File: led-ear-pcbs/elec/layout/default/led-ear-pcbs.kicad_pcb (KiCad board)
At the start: 2 copper layers, 225.7 x 100.8 mm, 0 parts

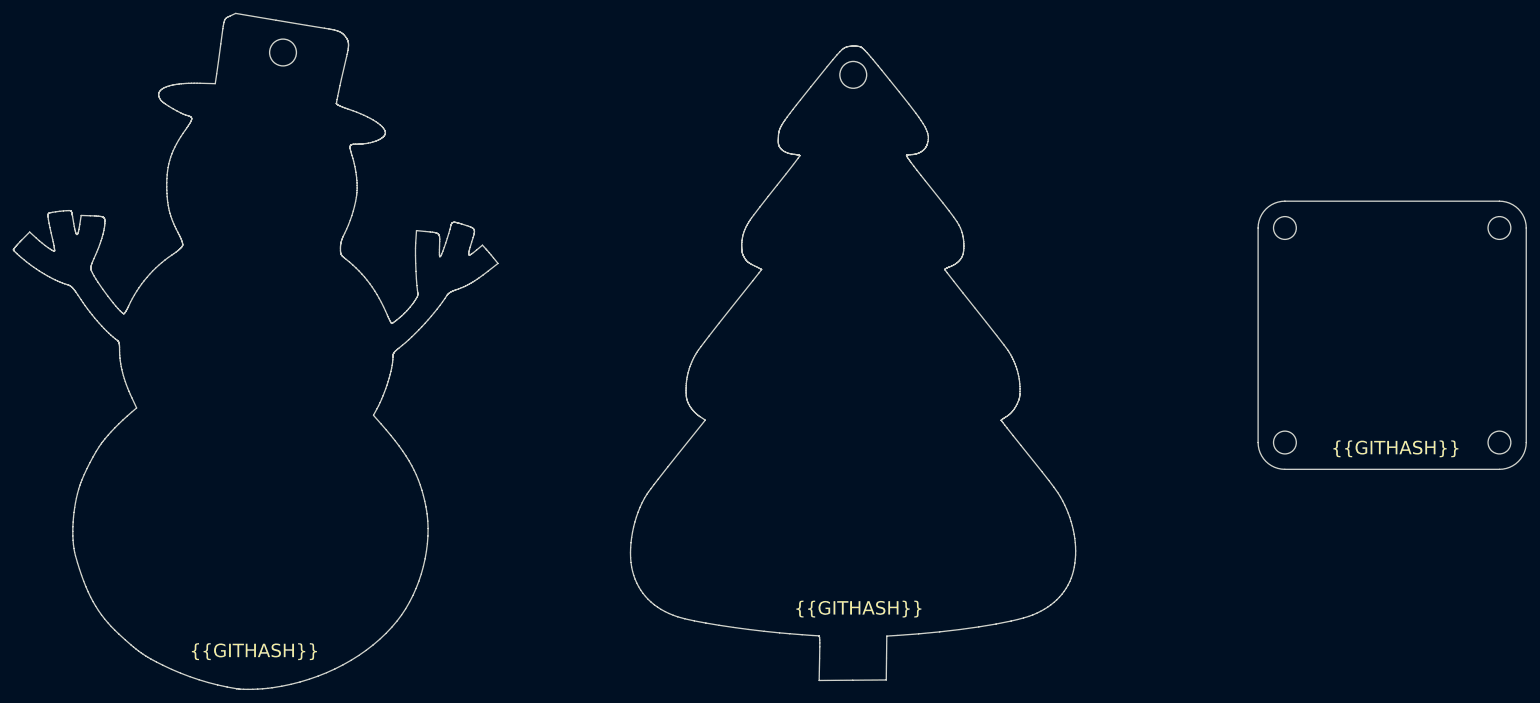
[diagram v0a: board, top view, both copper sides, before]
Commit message: added all components and specs, starting placing components
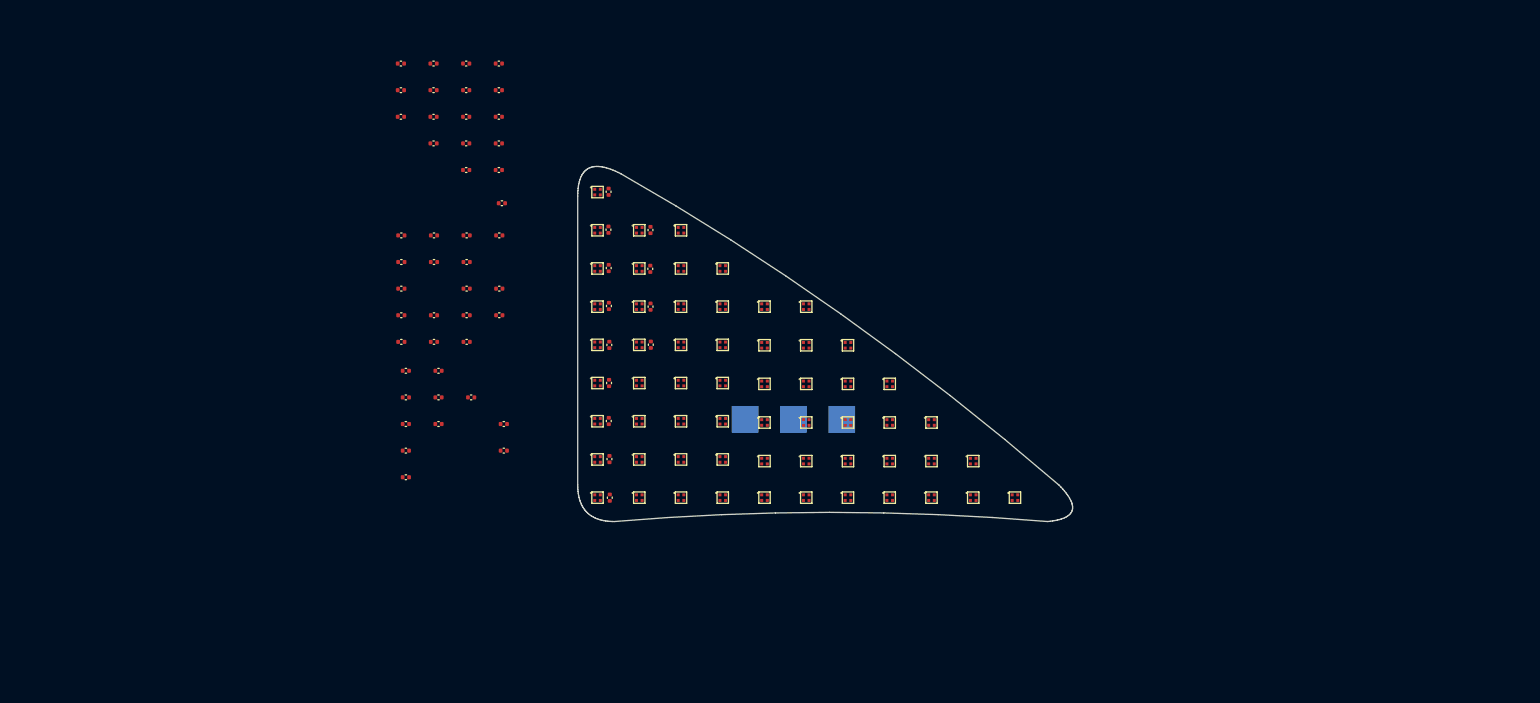
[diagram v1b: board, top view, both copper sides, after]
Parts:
- added C1: 16V 100nF X7R ±10% 0402 Multilayer Ceramic Capacitors MLCC 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, lib:C0402, F.Cu at (99.4, 103.1)
- added C10: 16V 100nF X7R ±10% 0402 Multilayer Ceramic Capacitors MLCC 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, lib:C0402, F.Cu at (131.0, 82.1)
- added C11: 16V 100nF X7R ±10% 0402 Multilayer Ceramic Capacitors MLCC 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, lib:C0402, F.Cu at (130.9, 87.9)
- added C12: 16V 100nF X7R ±10% 0402 Multilayer Ceramic Capacitors MLCC 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, lib:C0402, F.Cu at (131.0, 93.5)
- added C13: 16V 100nF X7R ±10% 0402 Multilayer Ceramic Capacitors MLCC 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, lib:C0402, F.Cu at (131.0, 99.2)
- added C14: 16V 100nF X7R ±10% 0402 Multilayer Ceramic Capacitors MLCC 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, lib:C0402, F.Cu at (94.5, 111.0)
- added C15: 16V 100nF X7R ±10% 0402 Multilayer Ceramic Capacitors MLCC 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, lib:C0402, F.Cu at (124.9, 122.0)
- added C16: 16V 100nF X7R ±10% 0402 Multilayer Ceramic Capacitors MLCC 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, lib:C0402, F.Cu at (99.4, 111.0)
- added C17: 16V 100nF X7R ±10% 0402 Multilayer Ceramic Capacitors MLCC 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, lib:C0402, F.Cu at (104.2, 107.1)
- added C18: 16V 100nF X7R ±10% 0402 Multilayer Ceramic Capacitors MLCC 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, lib:C0402, F.Cu at (109.1, 115.0)
- added C19: 16V 100nF X7R ±10% 0402 Multilayer Ceramic Capacitors MLCC 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, lib:C0402, F.Cu at (99.4, 107.1)
- added C2: 16V 100nF X7R ±10% 0402 Multilayer Ceramic Capacitors MLCC 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, lib:C0402, F.Cu at (94.5, 107.1)
- added C20: 16V 100nF X7R ±10% 0402 Multilayer Ceramic Capacitors MLCC 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, lib:C0402, F.Cu at (94.5, 115.0)
- added C21: 16V 100nF X7R ±10% 0402 Multilayer Ceramic Capacitors MLCC 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, lib:C0402, F.Cu at (124.9, 116.3)
- added C22: 16V 100nF X7R ±10% 0402 Multilayer Ceramic Capacitors MLCC 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, lib:C0402, F.Cu at (93.8, 82.9)
- added C23: 16V 100nF X7R ±10% 0402 Multilayer Ceramic Capacitors MLCC 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, lib:C0402, F.Cu at (108.4, 94.8)
- added C24: 16V 100nF X7R ±10% 0402 Multilayer Ceramic Capacitors MLCC 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, lib:C0402, F.Cu at (93.8, 86.9)
- added C25: 16V 100nF X7R ±10% 0402 Multilayer Ceramic Capacitors MLCC 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, lib:C0402, F.Cu at (103.6, 86.9)
- added C26: 16V 100nF X7R ±10% 0402 Multilayer Ceramic Capacitors MLCC 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, lib:C0402, F.Cu at (93.8, 98.8)
- added C27: 16V 100nF X7R ±10% 0402 Multilayer Ceramic Capacitors MLCC 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, lib:C0402, F.Cu at (103.6, 82.9)
- added C28: 16V 100nF X7R ±10% 0402 Multilayer Ceramic Capacitors MLCC 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, lib:C0402, F.Cu at (93.8, 90.8)
- added C29: 16V 100nF X7R ±10% 0402 Multilayer Ceramic Capacitors MLCC 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, lib:C0402, F.Cu at (98.7, 82.9)
- added C3: 16V 100nF X7R ±10% 0402 Multilayer Ceramic Capacitors MLCC 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, lib:C0402, F.Cu at (94.5, 119.0)
- added C30: 16V 100nF X7R ±10% 0402 Multilayer Ceramic Capacitors MLCC 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, lib:C0402, F.Cu at (98.7, 86.9)
- added C31: 16V 100nF X7R ±10% 0402 Multilayer Ceramic Capacitors MLCC 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, lib:C0402, F.Cu at (103.6, 90.8)
- added C32: 16V 100nF X7R ±10% 0402 Multilayer Ceramic Capacitors MLCC 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, lib:C0402, F.Cu at (108.4, 90.8)
- added C33: 16V 100nF X7R ±10% 0402 Multilayer Ceramic Capacitors MLCC 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, lib:C0402, F.Cu at (98.7, 98.8)
- added C34: 16V 100nF X7R ±10% 0402 Multilayer Ceramic Capacitors MLCC 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, lib:C0402, F.Cu at (103.6, 98.8)
- added C35: 16V 100nF X7R ±10% 0402 Multilayer Ceramic Capacitors MLCC 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, lib:C0402, F.Cu at (108.8, 78.1)
- added C36: 16V 100nF X7R ±10% 0402 Multilayer Ceramic Capacitors MLCC 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, lib:C0402, F.Cu at (93.8, 94.8)
- added C37: 16V 100nF X7R ±10% 0402 Multilayer Ceramic Capacitors MLCC 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, lib:C0402, F.Cu at (98.7, 94.8)
- added C38: 16V 100nF X7R ±10% 0402 Multilayer Ceramic Capacitors MLCC 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, lib:C0402, F.Cu at (108.4, 82.9)
- added C39: 16V 100nF X7R ±10% 0402 Multilayer Ceramic Capacitors MLCC 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, lib:C0402, F.Cu at (124.8, 110.6)
- added C4: 16V 100nF X7R ±10% 0402 Multilayer Ceramic Capacitors MLCC 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, lib:C0402, F.Cu at (109.1, 111.0)
- added C40: 16V 100nF X7R ±10% 0402 Multilayer Ceramic Capacitors MLCC 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, lib:C0402, F.Cu at (103.6, 94.8)
- added C41: 16V 100nF X7R ±10% 0402 Multilayer Ceramic Capacitors MLCC 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, lib:C0402, F.Cu at (124.8, 104.9)
- added C42: 16V 100nF X7R ±10% 0402 Multilayer Ceramic Capacitors MLCC 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, lib:C0402, F.Cu at (108.4, 57.3)
- added C43: 16V 100nF X7R ±10% 0402 Multilayer Ceramic Capacitors MLCC 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, lib:C0402, F.Cu at (103.5, 65.2)
- added C44: 16V 100nF X7R ±10% 0402 Multilayer Ceramic Capacitors MLCC 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, lib:C0402, F.Cu at (103.5, 73.1)
- added C45: 16V 100nF X7R ±10% 0402 Multilayer Ceramic Capacitors MLCC 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, lib:C0402, F.Cu at (98.6, 65.2)
- added C46: 16V 100nF X7R ±10% 0402 Multilayer Ceramic Capacitors MLCC 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, lib:C0402, F.Cu at (108.4, 65.2)
- added C47: 16V 100nF X7R ±10% 0402 Multilayer Ceramic Capacitors MLCC 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, lib:C0402, F.Cu at (103.5, 69.2)
- added C48: 16V 100nF X7R ±10% 0402 Multilayer Ceramic Capacitors MLCC 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, lib:C0402, F.Cu at (108.4, 73.1)
- added C49: 16V 100nF X7R ±10% 0402 Multilayer Ceramic Capacitors MLCC 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, lib:C0402, F.Cu at (98.6, 69.2)
- added C5: 16V 100nF X7R ±10% 0402 Multilayer Ceramic Capacitors MLCC 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, lib:C0402, F.Cu at (94.5, 103.1)
- added C50: 16V 100nF X7R ±10% 0402 Multilayer Ceramic Capacitors MLCC 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, lib:C0402, F.Cu at (93.8, 65.2)
- added C51: 16V 100nF X7R ±10% 0402 Multilayer Ceramic Capacitors MLCC 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, lib:C0402, F.Cu at (98.6, 57.3)
- added C52: 16V 100nF X7R ±10% 0402 Multilayer Ceramic Capacitors MLCC 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, lib:C0402, F.Cu at (108.4, 61.2)
- added C53: 16V 100nF X7R ±10% 0402 Multilayer Ceramic Capacitors MLCC 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, lib:C0402, F.Cu at (93.8, 61.2)
- added C54: 16V 100nF X7R ±10% 0402 Multilayer Ceramic Capacitors MLCC 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, lib:C0402, F.Cu at (98.6, 61.2)
- added C55: 16V 100nF X7R ±10% 0402 Multilayer Ceramic Capacitors MLCC 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, lib:C0402, F.Cu at (103.5, 61.2)
- added C56: 16V 100nF X7R ±10% 0402 Multilayer Ceramic Capacitors MLCC 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, lib:C0402, F.Cu at (103.5, 57.3)
- added C57: 16V 100nF X7R ±10% 0402 Multilayer Ceramic Capacitors MLCC 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, lib:C0402, F.Cu at (93.8, 57.3)
- added C58: 16V 100nF X7R ±10% 0402 Multilayer Ceramic Capacitors MLCC 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, lib:C0402, F.Cu at (108.4, 69.2)
- added C59: 16V 100nF X7R ±10% 0402 Multilayer Ceramic Capacitors MLCC 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, lib:C0402, F.Cu at (124.8, 99.2)
- added C6: 16V 100nF X7R ±10% 0402 Multilayer Ceramic Capacitors MLCC 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, lib:C0402, F.Cu at (124.8, 93.4)
- added C7: 16V 100nF X7R ±10% 0402 Multilayer Ceramic Capacitors MLCC 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, lib:C0402, F.Cu at (124.8, 87.8)
- added C8: 16V 100nF X7R ±10% 0402 Multilayer Ceramic Capacitors MLCC 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, lib:C0402, F.Cu at (124.7, 82.0)
- added C9: 16V 100nF X7R ±10% 0402 Multilayer Ceramic Capacitors MLCC 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, lib:C0402, F.Cu at (124.7, 76.4)
- added U1: , lib:TestPoint_Pad_4.0x4.0mm, B.Cu at (159.5, 110.3)
- added U10: , lib:LED-SMD_4P-L1.0-W1.0-TL_XL-1010RGBC-WS2812B, F.Cu at (123.1, 87.8)
- added U11: , lib:LED-SMD_4P-L1.0-W1.0-TL_XL-1010RGBC-WS2812B, F.Cu at (123.1, 82.1)
- added U12: , lib:LED-SMD_4P-L1.0-W1.0-TL_XL-1010RGBC-WS2812B, F.Cu at (123.1, 76.4)
- added U13: , lib:LED-SMD_4P-L1.0-W1.0-TL_XL-1010RGBC-WS2812B, F.Cu at (129.3, 82.1)
- added U14: , lib:LED-SMD_4P-L1.0-W1.0-TL_XL-1010RGBC-WS2812B, F.Cu at (129.3, 87.8)
- added U15: , lib:LED-SMD_4P-L1.0-W1.0-TL_XL-1010RGBC-WS2812B, F.Cu at (129.3, 93.5)
- added U16: , lib:LED-SMD_4P-L1.0-W1.0-TL_XL-1010RGBC-WS2812B, F.Cu at (129.3, 99.2)
- added U17: , lib:LED-SMD_4P-L1.0-W1.0-TL_XL-1010RGBC-WS2812B, F.Cu at (129.3, 104.9)
- added U18: , lib:LED-SMD_4P-L1.0-W1.0-TL_XL-1010RGBC-WS2812B, F.Cu at (129.3, 110.6)
- added U19: , lib:LED-SMD_4P-L1.0-W1.0-TL_XL-1010RGBC-WS2812B, F.Cu at (129.3, 116.3)
- added U2: , lib:TestPoint_Pad_4.0x4.0mm, B.Cu at (152.3, 110.3)
- added U20: , lib:LED-SMD_4P-L1.0-W1.0-TL_XL-1010RGBC-WS2812B, F.Cu at (129.3, 122.0)
- added U21: , lib:LED-SMD_4P-L1.0-W1.0-TL_XL-1010RGBC-WS2812B, F.Cu at (135.5, 122.0)
- added U22: , lib:LED-SMD_4P-L1.0-W1.0-TL_XL-1010RGBC-WS2812B, F.Cu at (135.5, 116.3)
- added U23: , lib:LED-SMD_4P-L1.0-W1.0-TL_XL-1010RGBC-WS2812B, F.Cu at (135.5, 110.6)
- added U24: , lib:LED-SMD_4P-L1.0-W1.0-TL_XL-1010RGBC-WS2812B, F.Cu at (135.5, 104.9)
- added U25: , lib:LED-SMD_4P-L1.0-W1.0-TL_XL-1010RGBC-WS2812B, F.Cu at (135.5, 99.2)
- added U26: , lib:LED-SMD_4P-L1.0-W1.0-TL_XL-1010RGBC-WS2812B, F.Cu at (135.5, 93.5)
- added U27: , lib:LED-SMD_4P-L1.0-W1.0-TL_XL-1010RGBC-WS2812B, F.Cu at (135.5, 87.8)
- added U28: , lib:LED-SMD_4P-L1.0-W1.0-TL_XL-1010RGBC-WS2812B, F.Cu at (135.5, 82.1)
- added U29: , lib:LED-SMD_4P-L1.0-W1.0-TL_XL-1010RGBC-WS2812B, F.Cu at (141.8, 87.8)
- added U3: , lib:TestPoint_Pad_4.0x4.0mm, B.Cu at (145.1, 110.3)
- added U30: , lib:LED-SMD_4P-L1.0-W1.0-TL_XL-1010RGBC-WS2812B, F.Cu at (141.8, 93.5)
- added U31: , lib:LED-SMD_4P-L1.0-W1.0-TL_XL-1010RGBC-WS2812B, F.Cu at (141.8, 99.2)
- added U32: , lib:LED-SMD_4P-L1.0-W1.0-TL_XL-1010RGBC-WS2812B, F.Cu at (141.8, 104.9)
- added U33: , lib:LED-SMD_4P-L1.0-W1.0-TL_XL-1010RGBC-WS2812B, F.Cu at (141.8, 110.6)
- added U34: , lib:LED-SMD_4P-L1.0-W1.0-TL_XL-1010RGBC-WS2812B, F.Cu at (141.8, 116.3)
- added U35: , lib:LED-SMD_4P-L1.0-W1.0-TL_XL-1010RGBC-WS2812B, F.Cu at (141.8, 122.0)
- added U36: , lib:LED-SMD_4P-L1.0-W1.0-TL_XL-1010RGBC-WS2812B, F.Cu at (148.0, 122.0)
- added U37: , lib:LED-SMD_4P-L1.0-W1.0-TL_XL-1010RGBC-WS2812B, F.Cu at (148.0, 116.6)
- added U38: , lib:LED-SMD_4P-L1.0-W1.0-TL_XL-1010RGBC-WS2812B, F.Cu at (148.0, 110.8)
- added U39: , lib:LED-SMD_4P-L1.0-W1.0-TL_XL-1010RGBC-WS2812B, F.Cu at (148.0, 105.0)
- added U4: , lib:LED-SMD_4P-L1.0-W1.0-TL_XL-1010RGBC-WS2812B, F.Cu at (123.1, 122.0)
- added U40: , lib:LED-SMD_4P-L1.0-W1.0-TL_XL-1010RGBC-WS2812B, F.Cu at (148.0, 99.3)
- added U41: , lib:LED-SMD_4P-L1.0-W1.0-TL_XL-1010RGBC-WS2812B, F.Cu at (148.0, 93.5)
- added U42: , lib:LED-SMD_4P-L1.0-W1.0-TL_XL-1010RGBC-WS2812B, F.Cu at (154.2, 93.5)
- added U43: , lib:LED-SMD_4P-L1.0-W1.0-TL_XL-1010RGBC-WS2812B, F.Cu at (154.2, 99.3)
- added U44: , lib:LED-SMD_4P-L1.0-W1.0-TL_XL-1010RGBC-WS2812B, F.Cu at (154.2, 105.0)
- added U45: , lib:LED-SMD_4P-L1.0-W1.0-TL_XL-1010RGBC-WS2812B, F.Cu at (154.2, 110.8)
- added U46: , lib:LED-SMD_4P-L1.0-W1.0-TL_XL-1010RGBC-WS2812B, F.Cu at (154.2, 116.6)
- added U47: , lib:LED-SMD_4P-L1.0-W1.0-TL_XL-1010RGBC-WS2812B, F.Cu at (154.2, 122.0)
- added U48: , lib:LED-SMD_4P-L1.0-W1.0-TL_XL-1010RGBC-WS2812B, F.Cu at (160.4, 122.0)
- added U49: , lib:LED-SMD_4P-L1.0-W1.0-TL_XL-1010RGBC-WS2812B, F.Cu at (160.4, 116.6)
- added U5: , lib:LED-SMD_4P-L1.0-W1.0-TL_XL-1010RGBC-WS2812B, F.Cu at (123.1, 116.3)
- added U50: , lib:LED-SMD_4P-L1.0-W1.0-TL_XL-1010RGBC-WS2812B, F.Cu at (160.4, 110.8)
- added U51: , lib:LED-SMD_4P-L1.0-W1.0-TL_XL-1010RGBC-WS2812B, F.Cu at (160.4, 105.0)
- added U52: , lib:LED-SMD_4P-L1.0-W1.0-TL_XL-1010RGBC-WS2812B, F.Cu at (160.4, 99.3)
- added U53: , lib:LED-SMD_4P-L1.0-W1.0-TL_XL-1010RGBC-WS2812B, F.Cu at (166.7, 105.0)
- added U54: , lib:LED-SMD_4P-L1.0-W1.0-TL_XL-1010RGBC-WS2812B, F.Cu at (166.7, 110.8)
- added U55: , lib:LED-SMD_4P-L1.0-W1.0-TL_XL-1010RGBC-WS2812B, F.Cu at (166.7, 116.6)
- added U56: , lib:LED-SMD_4P-L1.0-W1.0-TL_XL-1010RGBC-WS2812B, F.Cu at (166.7, 122.0)
- added U57: , lib:LED-SMD_4P-L1.0-W1.0-TL_XL-1010RGBC-WS2812B, F.Cu at (172.9, 122.0)
- added U58: , lib:LED-SMD_4P-L1.0-W1.0-TL_XL-1010RGBC-WS2812B, F.Cu at (172.9, 116.6)
- added U59: , lib:LED-SMD_4P-L1.0-W1.0-TL_XL-1010RGBC-WS2812B, F.Cu at (172.9, 110.8)
- added U6: , lib:LED-SMD_4P-L1.0-W1.0-TL_XL-1010RGBC-WS2812B, F.Cu at (123.1, 110.6)
- added U60: , lib:LED-SMD_4P-L1.0-W1.0-TL_XL-1010RGBC-WS2812B, F.Cu at (179.1, 116.6)
- added U61: , lib:LED-SMD_4P-L1.0-W1.0-TL_XL-1010RGBC-WS2812B, F.Cu at (179.1, 122.0)
- added U62: , lib:LED-SMD_4P-L1.0-W1.0-TL_XL-1010RGBC-WS2812B, F.Cu at (185.3, 122.0)
- added U7: , lib:LED-SMD_4P-L1.0-W1.0-TL_XL-1010RGBC-WS2812B, F.Cu at (123.1, 104.9)
- added U8: , lib:LED-SMD_4P-L1.0-W1.0-TL_XL-1010RGBC-WS2812B, F.Cu at (123.1, 99.2)
- added U9: , lib:LED-SMD_4P-L1.0-W1.0-TL_XL-1010RGBC-WS2812B, F.Cu at (123.1, 93.5)
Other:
- board size 225.7 x 100.8 mm -> 73.8 x 53 mm
- board text removed: "{{GITHASH}}"

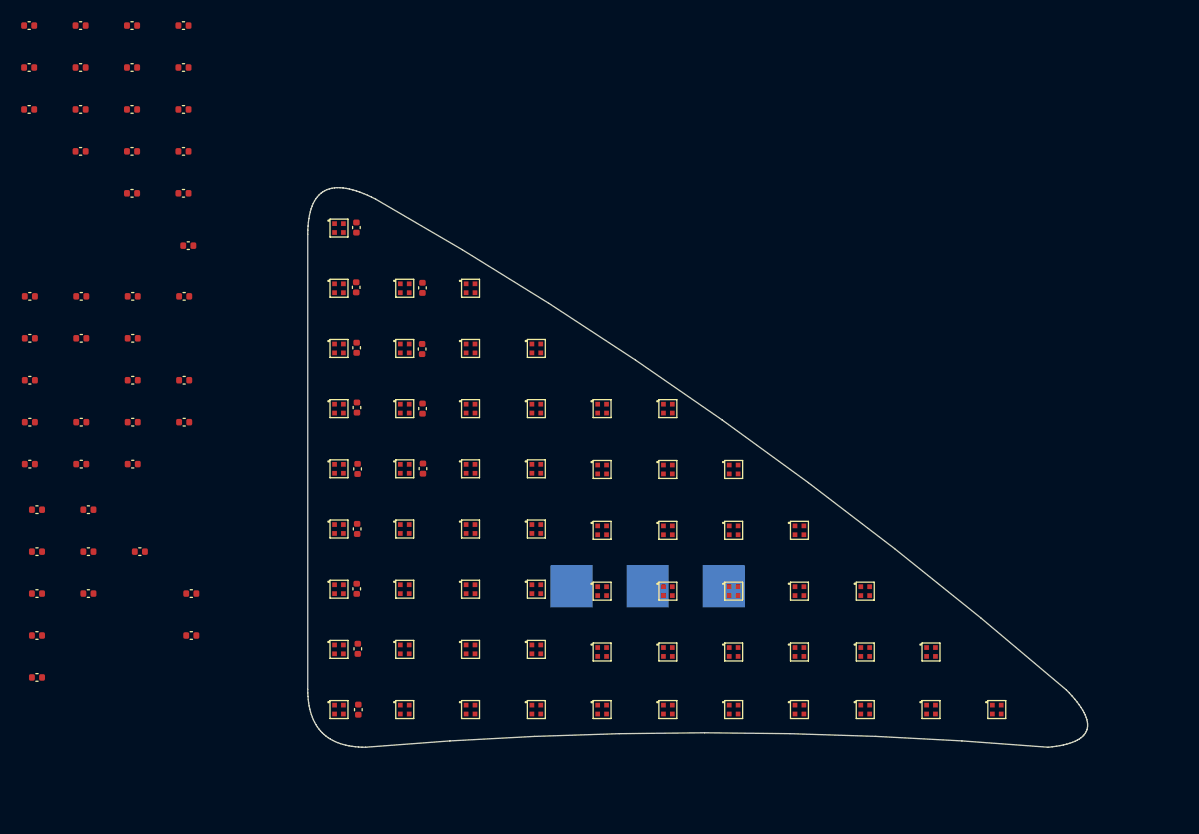
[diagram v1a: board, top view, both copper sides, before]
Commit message: made progress with routing pcb
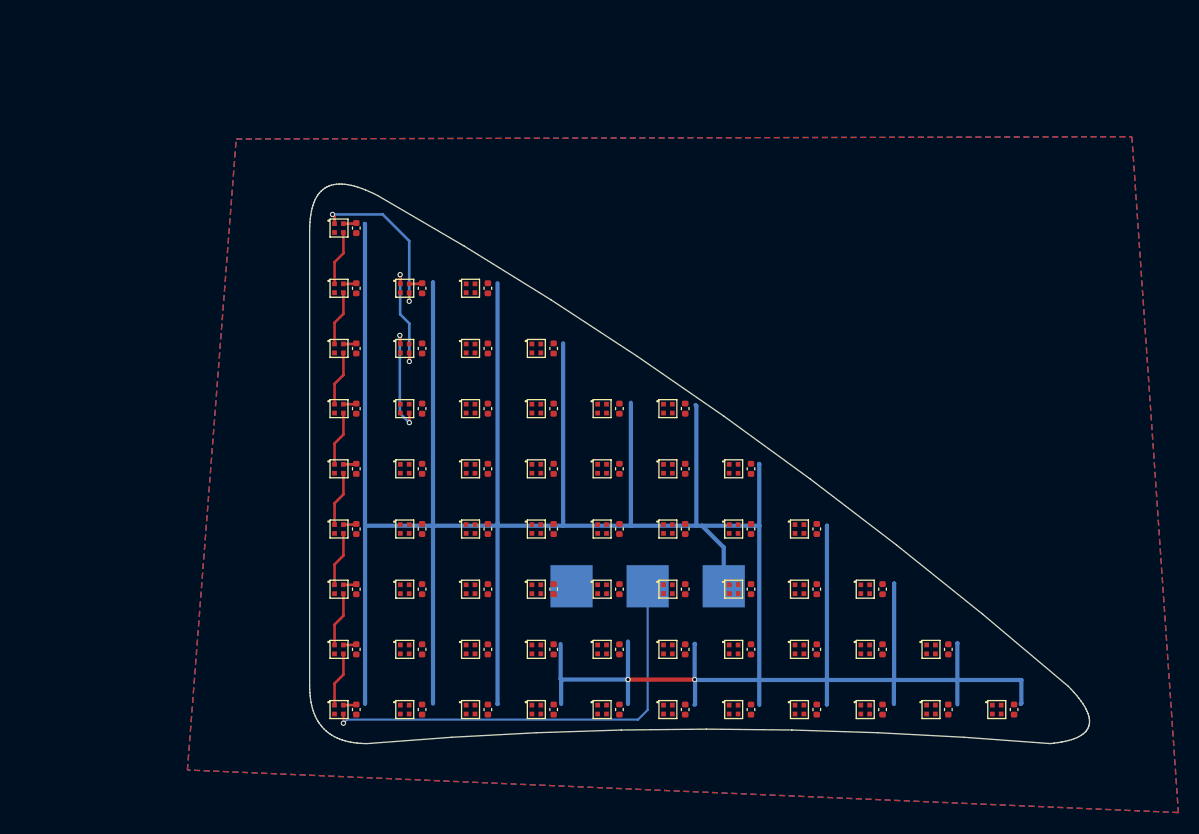
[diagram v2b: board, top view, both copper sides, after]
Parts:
- moved C57 105.2 mm to (180.8, 116.3), turned to -90 degrees
- moved C54 97.2 mm to (174.5, 122.0), turned to -90 degrees
- moved C53 96.2 mm to (168.3, 122.0), turned to -90 degrees
- moved C55 89.9 mm to (174.5, 116.3), turned to -90 degrees
- moved C58 89.6 mm to (180.8, 122.0), turned to -90 degrees
- moved C56 88.8 mm to (174.5, 110.6), turned to -90 degrees
- moved C51 87.8 mm to (168.3, 110.6), turned to -90 degrees
- moved C45 85.2 mm to (162.1, 122.0), turned to -90 degrees
- moved C50 84.5 mm to (168.3, 104.9), turned to -90 degrees
- moved C52 81.4 mm to (168.3, 116.3), turned to -90 degrees
- moved C46 74.2 mm to (162.1, 116.3), turned to -90 degrees
- moved C43 73.2 mm to (155.9, 116.3), turned to -90 degrees
- moved C47 71.8 mm to (162.1, 110.6), turned to -90 degrees
- moved C44 71.6 mm to (155.9, 122.0), turned to -90 degrees
- moved C42 71.4 mm to (155.9, 110.6), turned to -90 degrees
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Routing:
- net vcc: track 0.00 -> 342.3 mm, vias 0 -> 2
- net din: track 0.00 -> 41.9 mm, vias 0 -> 1
- net led_9-dout: track 0.00 -> 15.8 mm, vias 0 -> 2
- net led_11-dout: track 0.00 -> 10.4 mm, vias 0 -> 2
- net led_10-dout: track 0.00 -> 10.3 mm, vias 0 -> 2
- net led_5-dout: track 0.00 -> 5.21 mm
- net led_8-dout: track 0.00 -> 5.21 mm
- net led_7-dout: track 0.00 -> 5.21 mm
- net led_6-dout: track 0.00 -> 5.21 mm
- net led_4-dout: track 0.00 -> 5.21 mm
- net led_2-dout: track 0.00 -> 5.21 mm
- net led_1-dout: track 0.00 -> 5.21 mm
- net led_3-dout: track 0.00 -> 5.21 mm
- added copper zone on B.Cu, net gnd
- added copper zone on F.Cu, net gnd
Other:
- board text added: "5V"
- board text added: "D"
- board text added: "GND"

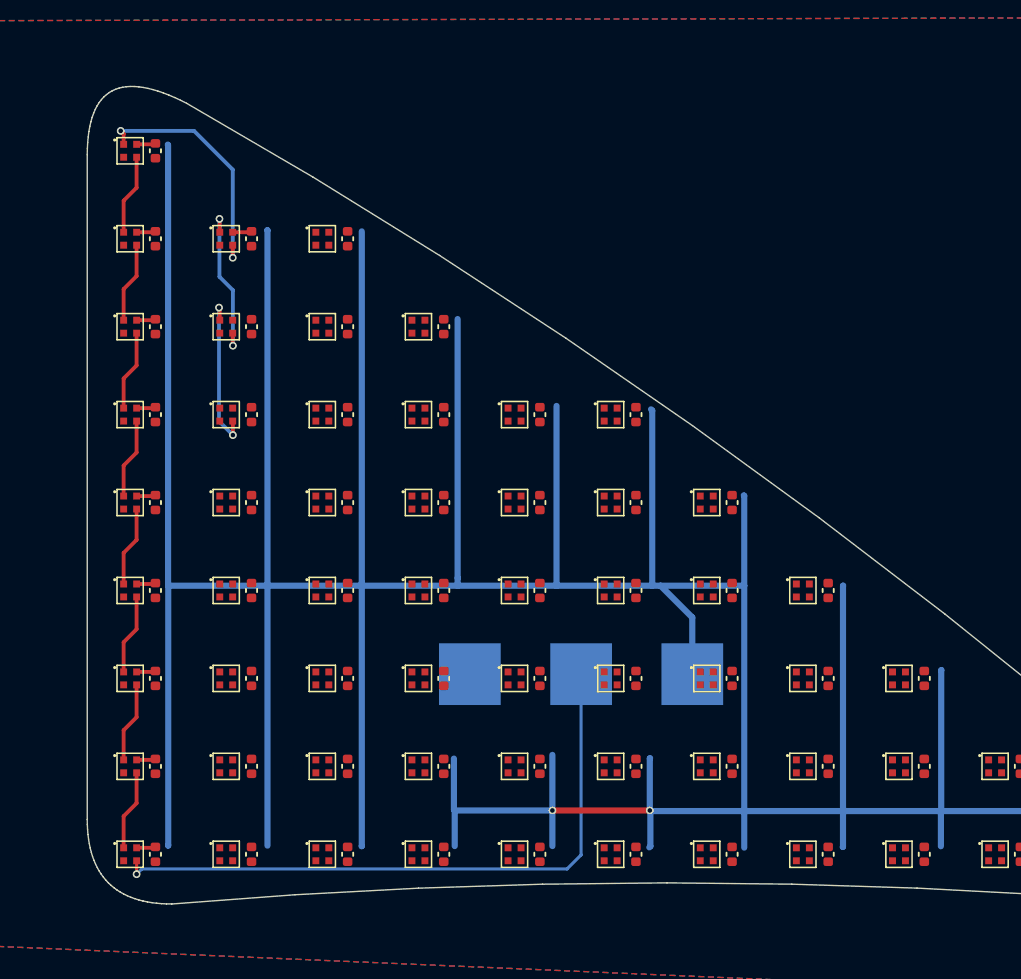
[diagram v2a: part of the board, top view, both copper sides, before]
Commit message: updated atopile, tried to fix crash
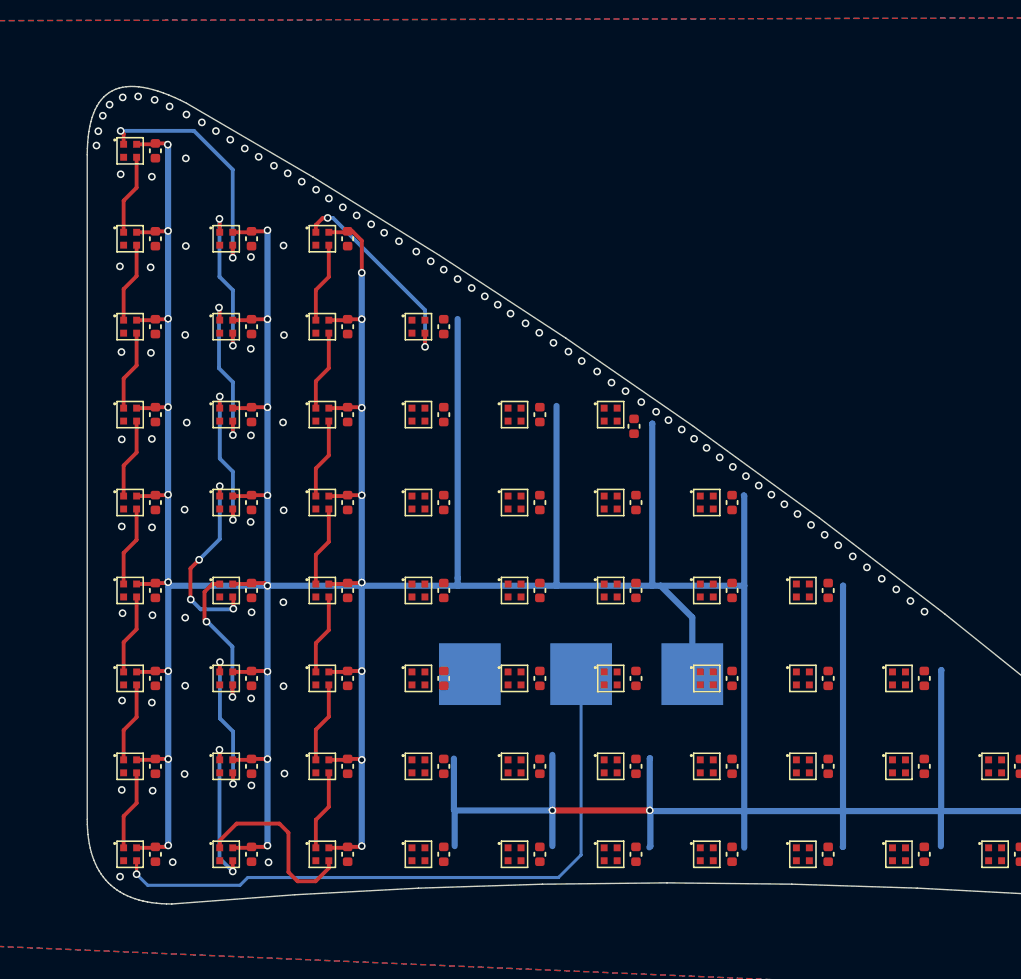
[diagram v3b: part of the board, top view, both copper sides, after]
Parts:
- moved C39 0.77 mm to (155.7, 94.3)
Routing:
- net vcc: track 342.3 -> 383.0 mm, vias 2 -> 27
- net led_25-dout: track 0.00 -> 13.5 mm, vias 0 -> 2
- net led_13-dout: track 0.00 -> 12.6 mm, vias 0 -> 4
- net led_17-dout: track 0.00 -> 11.9 mm
- net led_12-dout: track 0.00 -> 9.82 mm, vias 0 -> 2
- net led_15-dout: track 0.00 -> 9.61 mm, vias 0 -> 2
- net led_16-dout: track 0.00 -> 9.59 mm, vias 0 -> 2
- net led_14-dout: track 0.00 -> 9.59 mm, vias 0 -> 2
- net led_23-dout: track 0.00 -> 5.21 mm
- net led_21-dout: track 0.00 -> 5.21 mm
- net led_18-dout: track 0.00 -> 5.21 mm
- net led_24-dout: track 0.00 -> 5.21 mm
- net led_22-dout: track 0.00 -> 5.21 mm
- net led_19-dout: track 0.00 -> 5.21 mm
- net led_20-dout: track 0.00 -> 5.21 mm
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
